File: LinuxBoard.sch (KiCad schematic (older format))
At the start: 17 parts

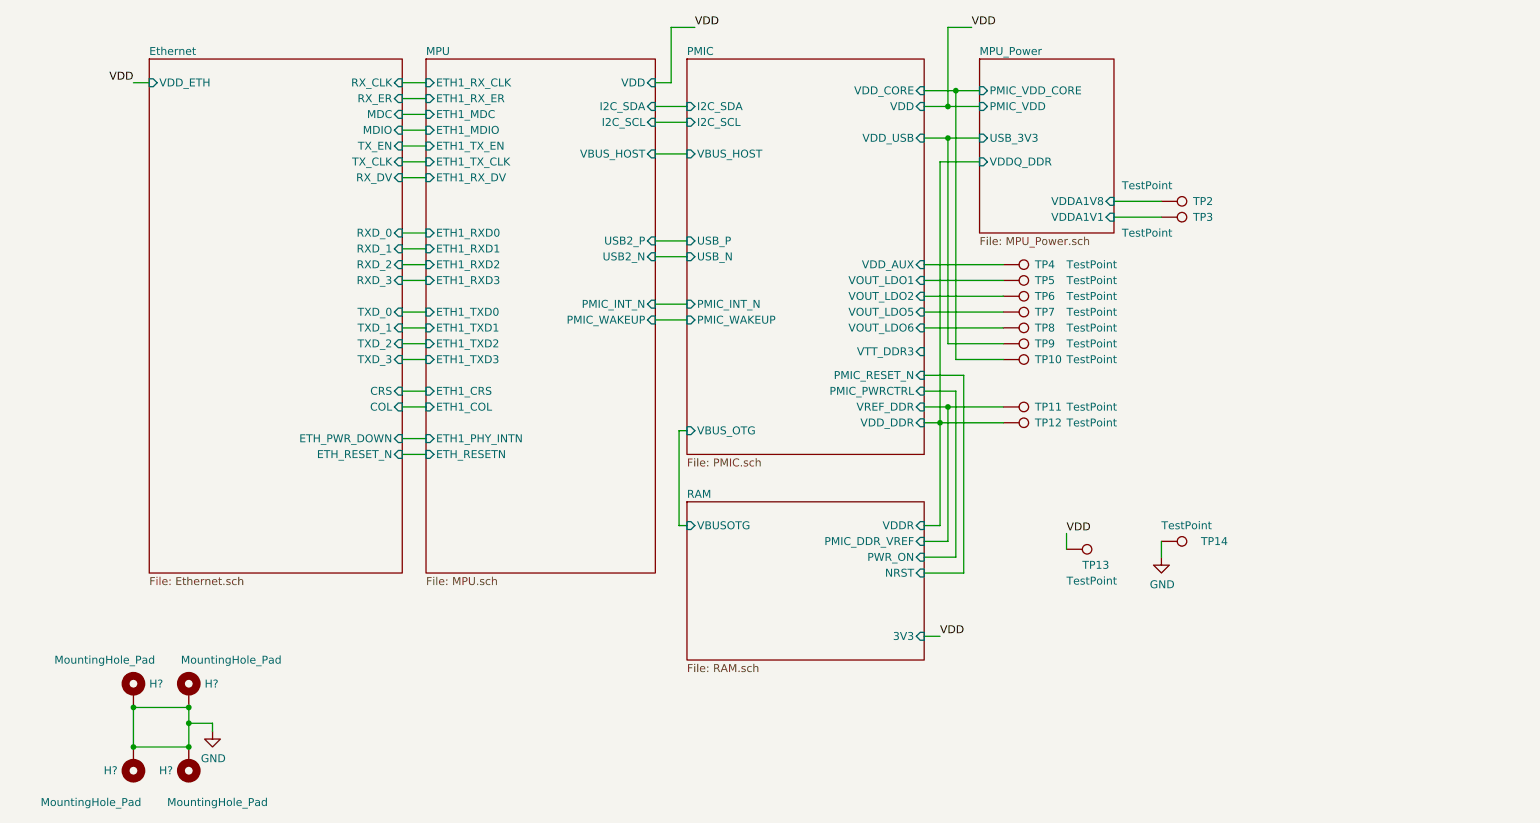
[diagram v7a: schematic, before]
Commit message: Add termination
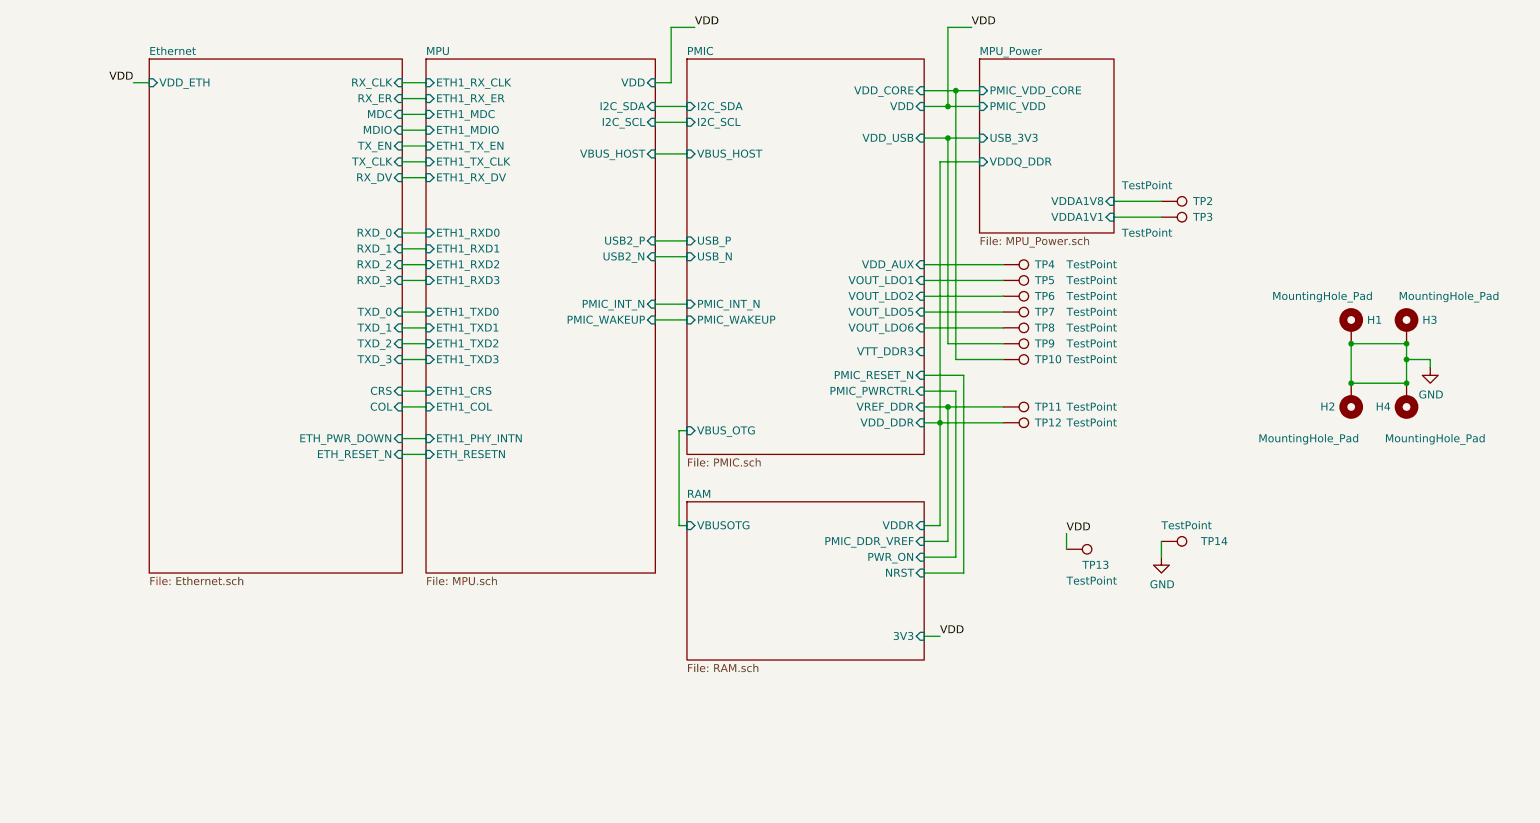
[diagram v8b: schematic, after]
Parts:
- H1, H2, H3, H4: renamed from H?; footprint (none) -> MountingHole:MountingHole_2.5mm_Pad
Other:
- moved on the sheet: H1, H2, H3, H4
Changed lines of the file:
@@
 	6950 2050 7100 2050
 $Comp
-L Mechanical:MountingHole_Pad H?
+L Mechanical:MountingHole_Pad H3
 U 1 1 60E8FE8D
-P 2100 5850
-F 0 "H?" H 2200 5899 50  0000 L CNN
-F 1 "MountingHole_Pad" H 2050 6050 50  0000 L CNN
-F 2 "" H 2100 5850 50  0001 C CNN
-F 3 "~" H 2100 5850 50  0001 C CNN
-	1    2100 5850
+P 9800 3550
+F 0 "H3" H 9900 3599 50  0000 L CNN
+F 1 "MountingHole_Pad" H 9750 3750 50  0000 L CNN
+F 2 "MountingHole:MountingHole_2.5mm_Pad" H 9800 3550 50  0001 C CNN
+F 3 "~" H 9800 3550 50  0001 C CNN
+	1    9800 3550
 	1    0    0    -1
 $EndComp
 $Comp
-L Mechanical:MountingHole_Pad H?
+L Mechanical:MountingHole_Pad H2
 U 1 1 60E9127A
-P 1750 6300
-F 0 "H?" H 1850 6349 50  0000 L CNN
-F 1 "MountingHole_Pad" H 1700 6550 50  0000 L CNN
-F 2 "" H 1750 6300 50  0001 C CNN
-F 3 "~" H 1750 6300 50  0001 C CNN
-	1    1750 6300
+P 9450 4000
+F 0 "H2" H 9550 4049 50  0000 L CNN
+F 1 "MountingHole_Pad" H 9400 4250 50  0000 L CNN
+F 2 "MountingHole:MountingHole_2.5mm_Pad" H 9450 4000 50  0001 C CNN
+F 3 "~" H 9450 4000 50  0001 C CNN
+	1    9450 4000
 	-1   0    0    1
 $EndComp
 $Comp
-L Mechanical:MountingHole_Pad H?
+L Mechanical:MountingHole_Pad H4
 U 1 1 60E9329A
-P 2100 6300
-F 0 "H?" H 2200 6349 50  0000 L CNN
-F 1 "MountingHole_Pad" H 1600 6550 50  0000 L CNN
-F 2 "" H 2100 6300 50  0001 C CNN
-F 3 "~" H 2100 6300 50  0001 C CNN
-	1    2100 6300
+P 9800 4000
+F 0 "H4" H 9900 4049 50  0000 L CNN
+F 1 "MountingHole_Pad" H 9300 4250 50  0000 L CNN
+F 2 "MountingHole:MountingHole_2.5mm_Pad" H 9800 4000 50  0001 C CNN
+F 3 "~" H 9800 4000 50  0001 C CNN
+	1    9800 4000
 	-1   0    0    1
 $EndComp
 $Comp
-L Mechanical:MountingHole_Pad H?
+L Mechanical:MountingHole_Pad H1
 U 1 1 60E95D0C
-P 1750 5850
-F 0 "H?" H 1850 5899 50  0000 L CNN
-F 1 "MountingHole_Pad" H 1250 6050 50  0000 L CNN
-F 2 "" H 1750 5850 50  0001 C CNN
-F 3 "~" H 1750 5850 50  0001 C CNN
-	1    1750 5850
+P 9450 3550
+F 0 "H1" H 9550 3599 50  0000 L CNN
+F 1 "MountingHole_Pad" H 8950 3750 50  0000 L CNN
+F 2 "MountingHole:MountingHole_2.5mm_Pad" H 9450 3550 50  0001 C CNN
+F 3 "~" H 9450 3550 50  0001 C CNN
+	1    9450 3550
 	1    0    0    -1
 $EndComp
 Wire Wire Line
-	2100 5950 1750 5950
+	9800 3650 9450 3650
 Wire Wire Line
-	1750 5950 1750 6200
-Connection ~ 1750 5950
+	9450 3650 9450 3900
+Connection ~ 9450 3650
 Wire Wire Line
-	1750 6200 2100 6200
+	9450 3900 9800 3900
 Wire Wire Line
-	2100 6200 2100 6050
-Connection ~ 1750 6200
-Connection ~ 2100 6200
-Connection ~ 2100 5950
+	9800 3900 9800 3750
+Connection ~ 9450 3900
+Connection ~ 9800 3900
+Connection ~ 9800 3650
 Wire Wire Line
-	2100 6050 2250 6050
+	9800 3750 9950 3750
 Wire Wire Line
-	2250 6050 2250 6100
-Connection ~ 2100 6050
+	9950 3750 9950 3800
+Connection ~ 9800 3750
 Wire Wire Line
-	2100 6050 2100 5950
+	9800 3750 9800 3650
 $Comp
-L power:GND #PWR?
+L power:GND #PWR032
 U 1 1 60E9D149
-P 2250 6100
-F 0 "#PWR?" H 2250 5850 50  0001 C CNN
-F 1 "GND" H 2255 5927 50  0000 C CNN
-F 2 "" H 2250 6100 50  0001 C CNN
-F 3 "" H 2250 6100 50  0001 C CNN
-	1    2250 6100
+P 9950 3800
+F 0 "#PWR032" H 9950 3550 50  0001 C CNN
+F 1 "GND" H 9955 3627 50  0000 C CNN
+F 2 "" H 9950 3800 50  0001 C CNN
+F 3 "" H 9950 3800 50  0001 C CNN
+	1    9950 3800
 	1    0    0    -1
 $EndComp
